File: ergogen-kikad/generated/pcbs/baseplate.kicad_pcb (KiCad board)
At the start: 2 copper layers, 111.1 x 55 mm, 16 parts

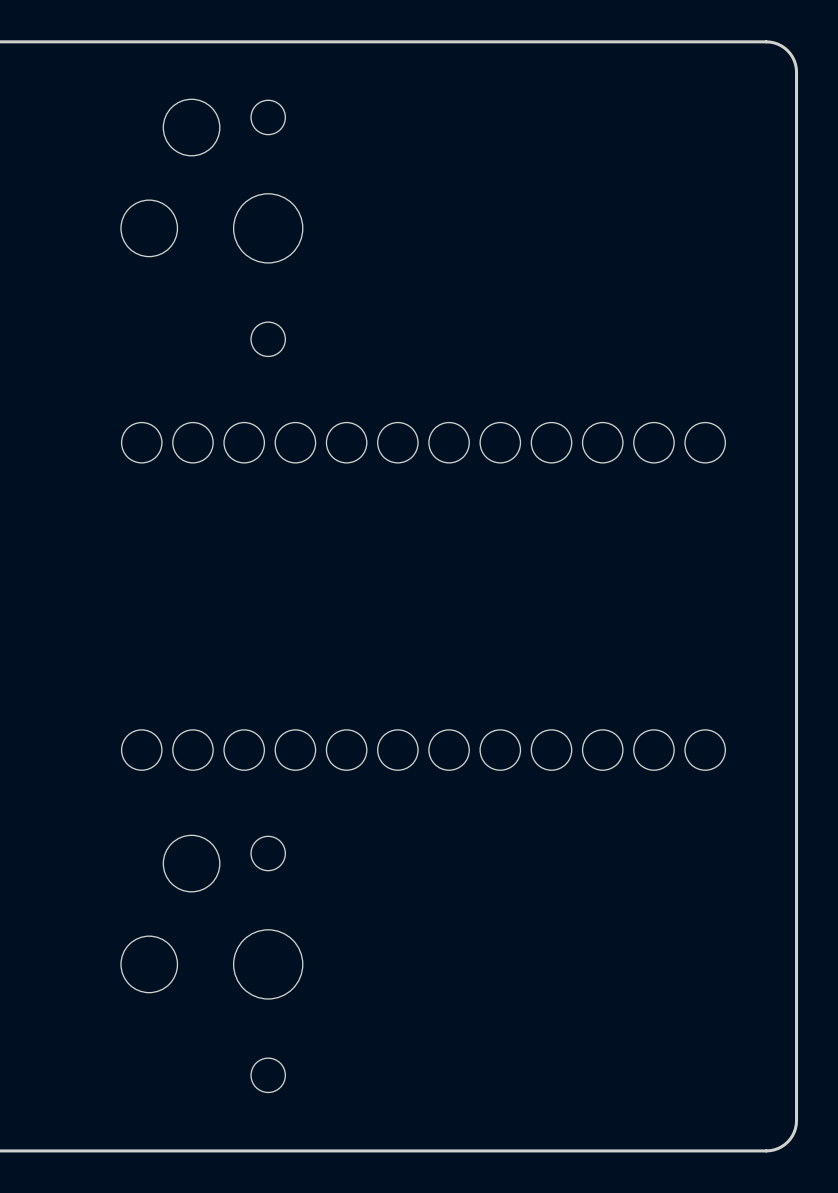
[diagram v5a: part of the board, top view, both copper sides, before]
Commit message: Use landscape fifth-column caps and add right-side mounting pair
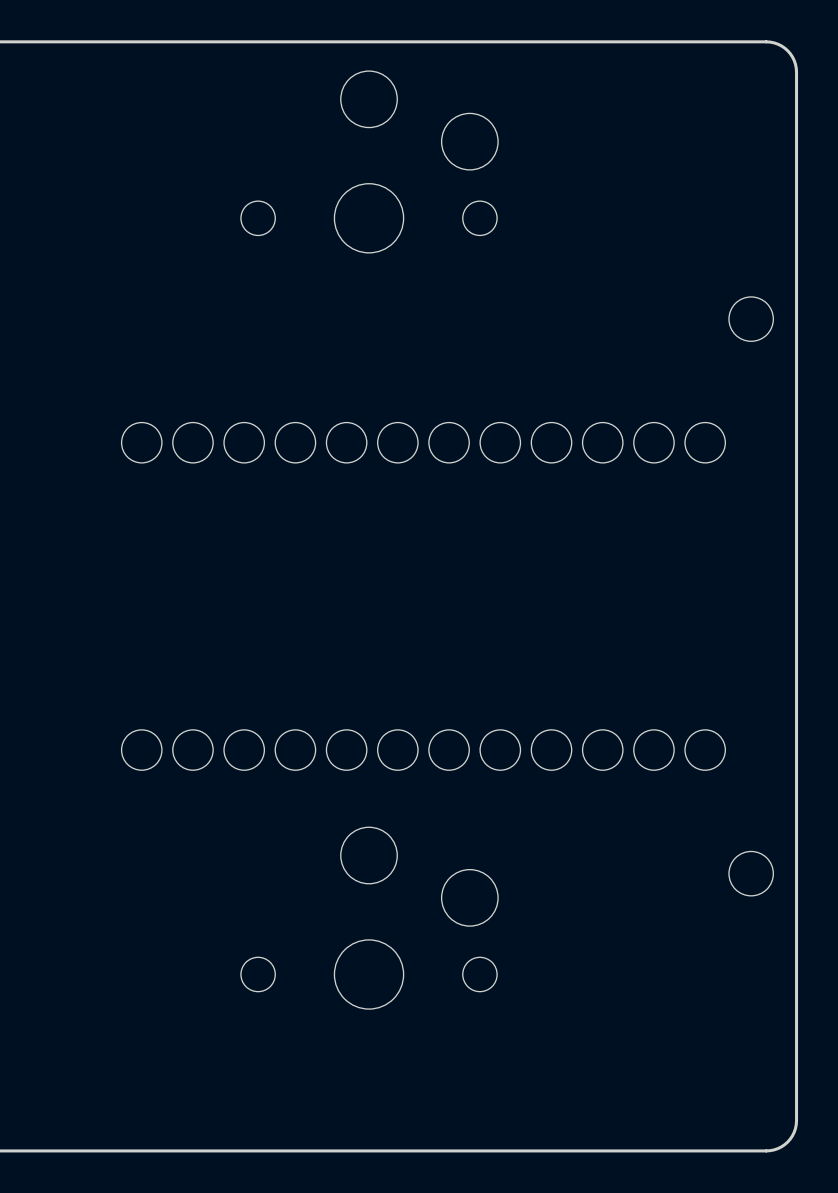
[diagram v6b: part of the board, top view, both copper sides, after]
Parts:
- added H5: M2 mount, M2_Mount, F.Cu at (263.3, 134.8)
- added H6: M2 mount, M2_Mount, F.Cu at (263.3, 162.2)
- S10, S9: value Choc v1 1U -> Choc v1 1.5U; footprint PG1350_1U -> PG1350_1_5U
- moved S10 5.02 mm to (244.4, 167.2), turned to 0 degrees
- moved S9 5.02 mm to (244.4, 129.8), turned to 0 degrees

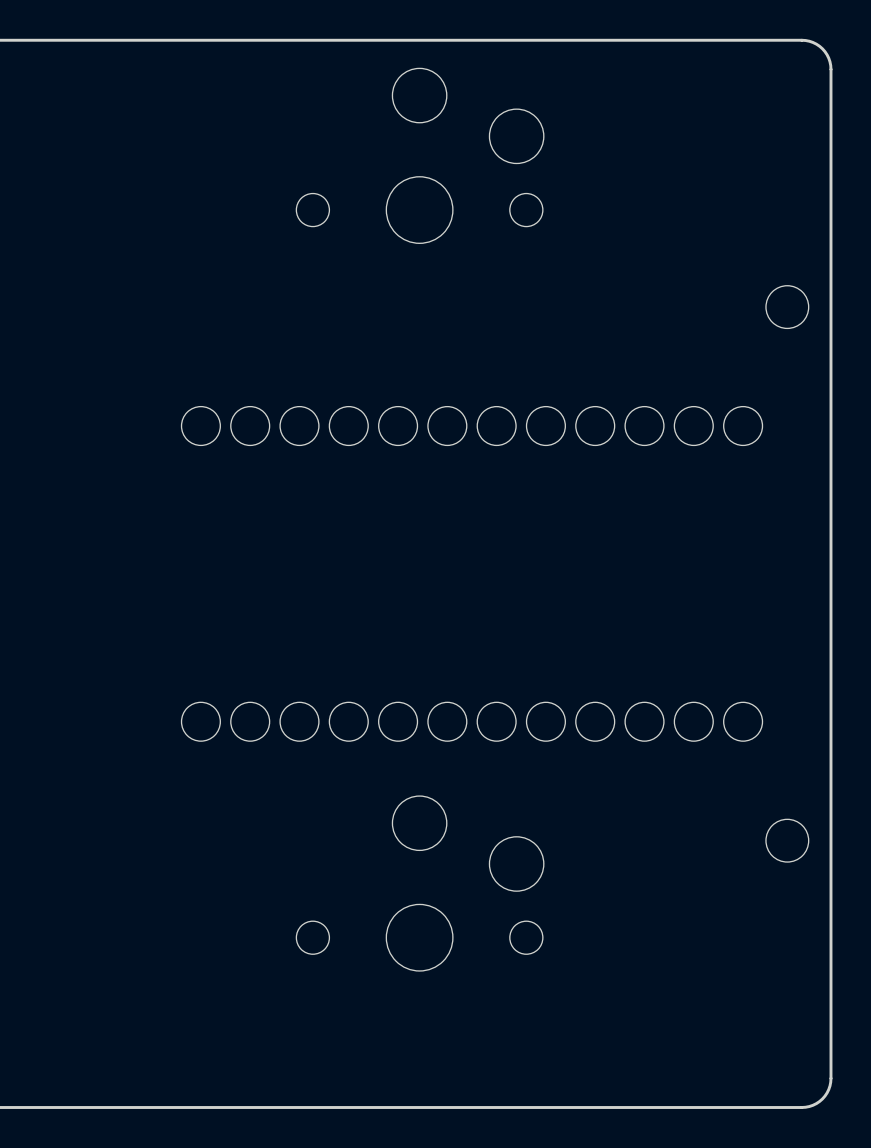
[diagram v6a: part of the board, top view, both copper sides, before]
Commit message: Add through-hole battery connector and top-facing power and reset controls
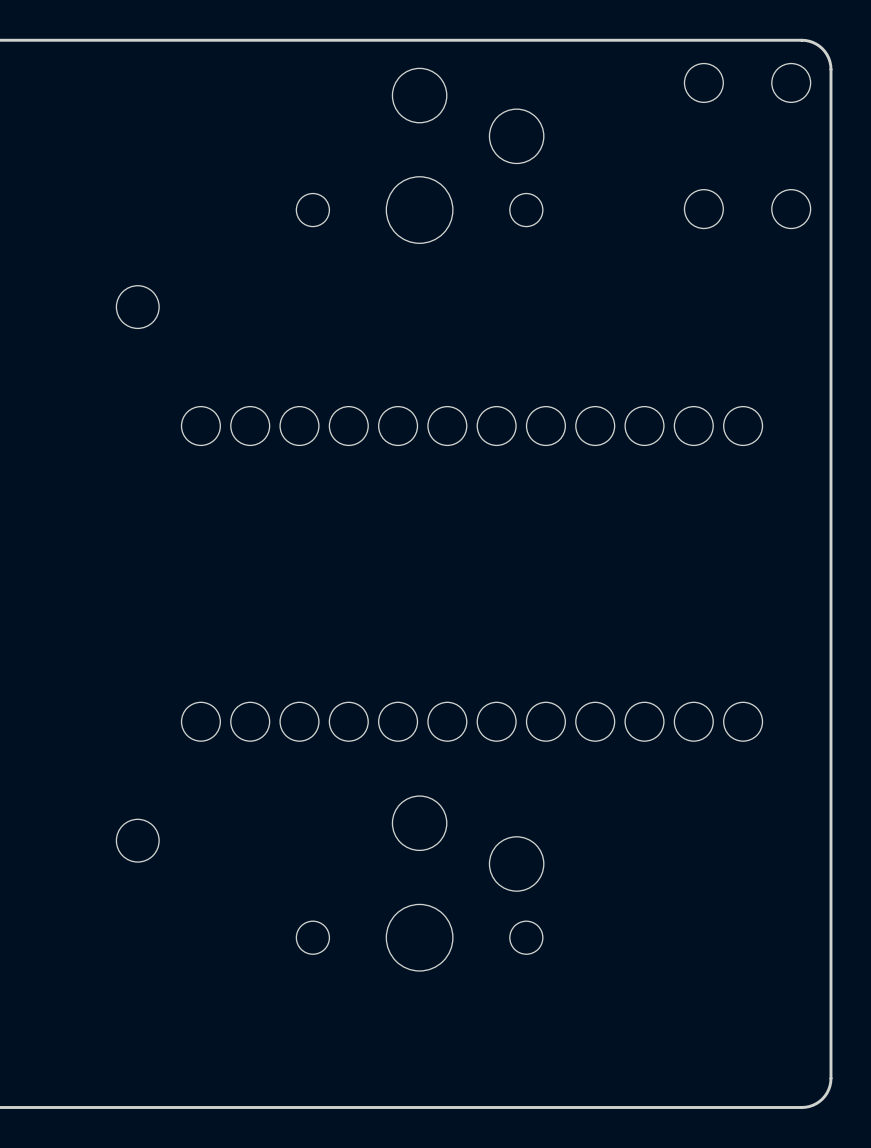
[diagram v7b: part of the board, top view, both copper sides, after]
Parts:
- added BAT1: 301230 110mAh max 32.5x12.5x3.2, Protected_301230_Battery_Envelope, F.Cu at (191.8, 148.5)
- added J1, PWR1: Header clearance, , F.Cu at (163.2, 162.2)
- added RST1: 6mm top-actuated tactile, SW_PUSH_6mm_H4_3mm, F.Cu at (261.3, 126.5)
- moved H5 33.5 mm to (229.8, 134.8)
- moved H6 33.5 mm to (229.8, 162.2)

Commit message: Reserve longer battery and export native KiCad assembly views
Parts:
- BAT1: value 301230 110mAh max 32.5x12.5x3.2 -> 301055 220mAh max 57.5x10.5x3.5; footprint Protected_301230_Battery_Envelope -> Protected_301055_Battery_Envelope
- moved BAT1 7.68 mm to (199.4, 148.5)
